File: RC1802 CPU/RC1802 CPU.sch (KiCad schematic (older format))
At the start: 50 parts, among them J1 Mount, J2 Mount, J3 Mount, J4 Mount, J5 CONN_01X39, J6 CONN_02X20, J7 BARREL_JACK, J8 Conn_CLK, J9 Conn_Q, U1 74LS04, U2 CDP1802, U3 74LS240, U4 74LS373, U5 SLOT-1, U6 SLOT-2, X1 CXO_DIP14

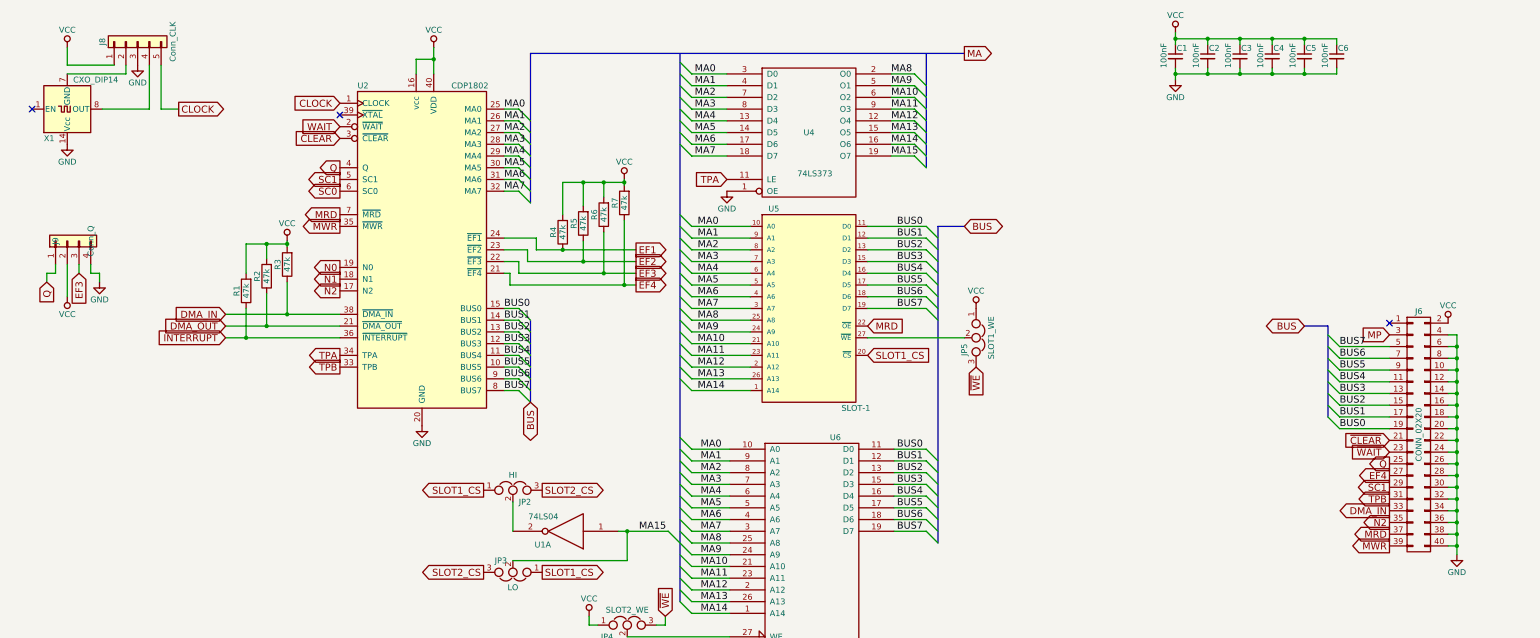
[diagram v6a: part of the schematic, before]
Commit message: Accidentally swapped VCC and GND on oscillator, no wonder it didn't work :-(
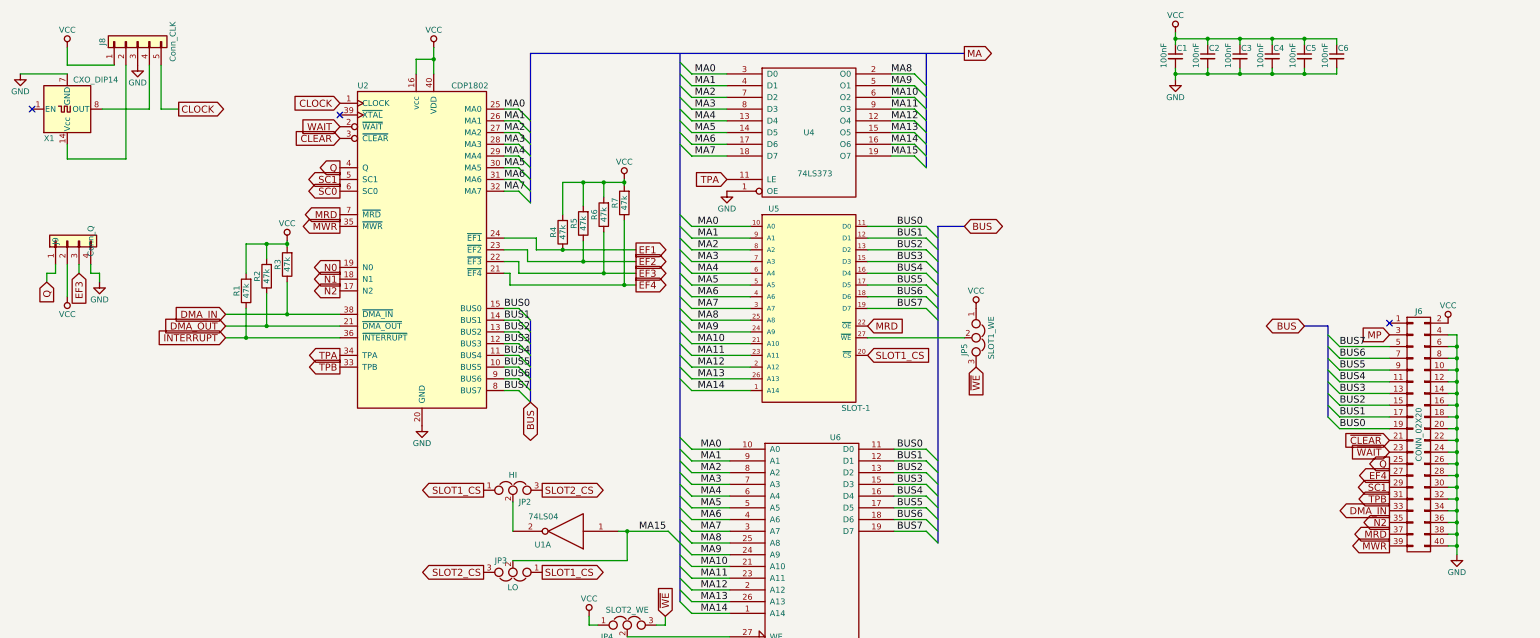
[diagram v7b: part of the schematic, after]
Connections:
- net GND: now also X1.7 (GND); no longer X1.14 (Vcc)
- net at J8.2 (Pin_2): now also X1.14 (Vcc); no longer X1.7 (GND)

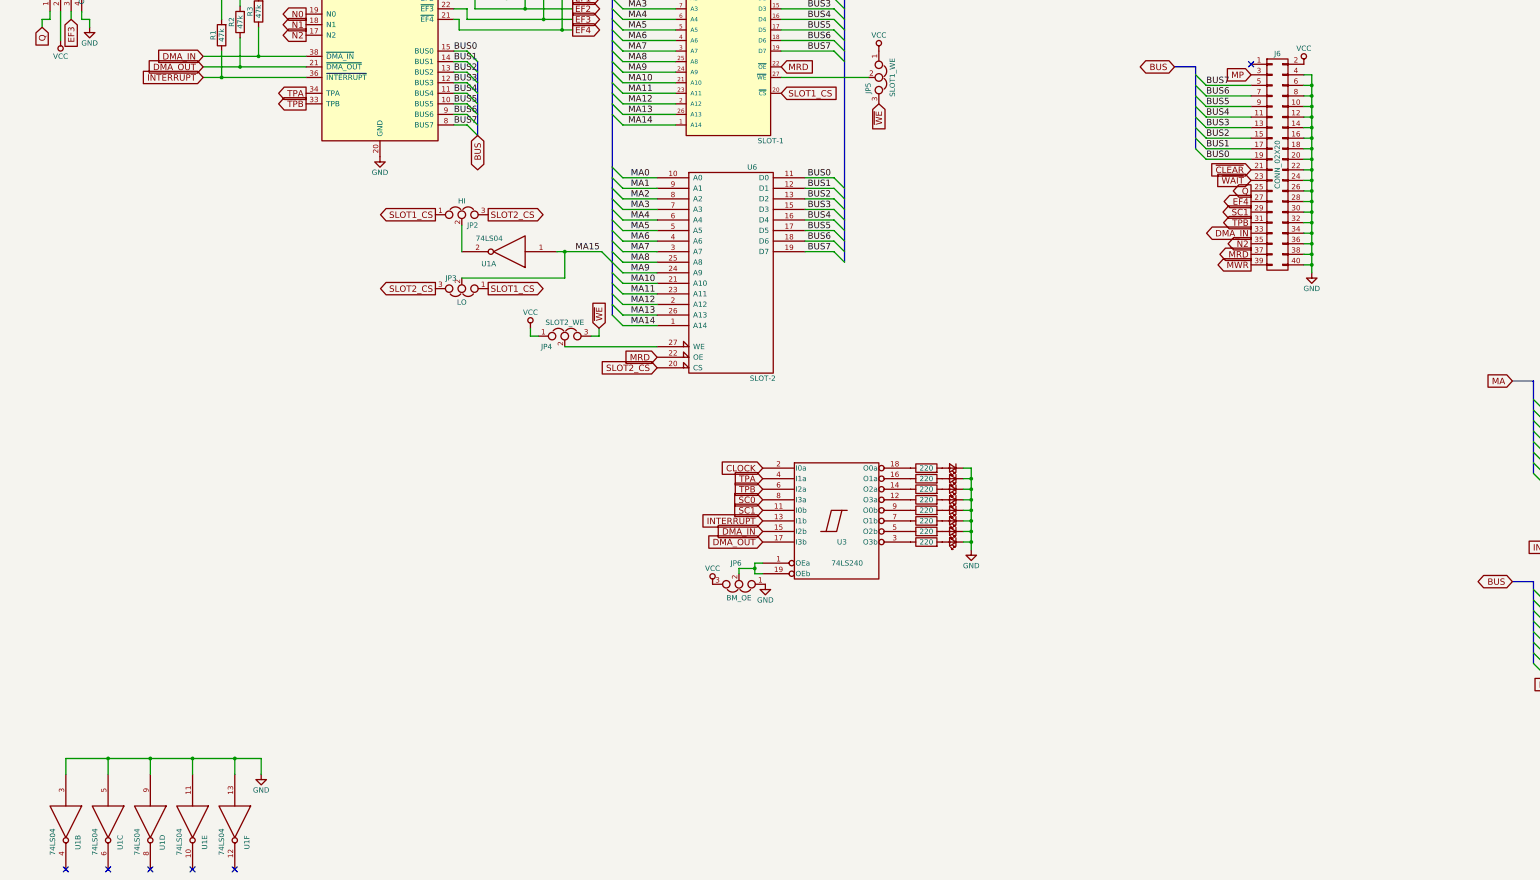
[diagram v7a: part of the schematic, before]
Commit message: Added ~Q to UI connector
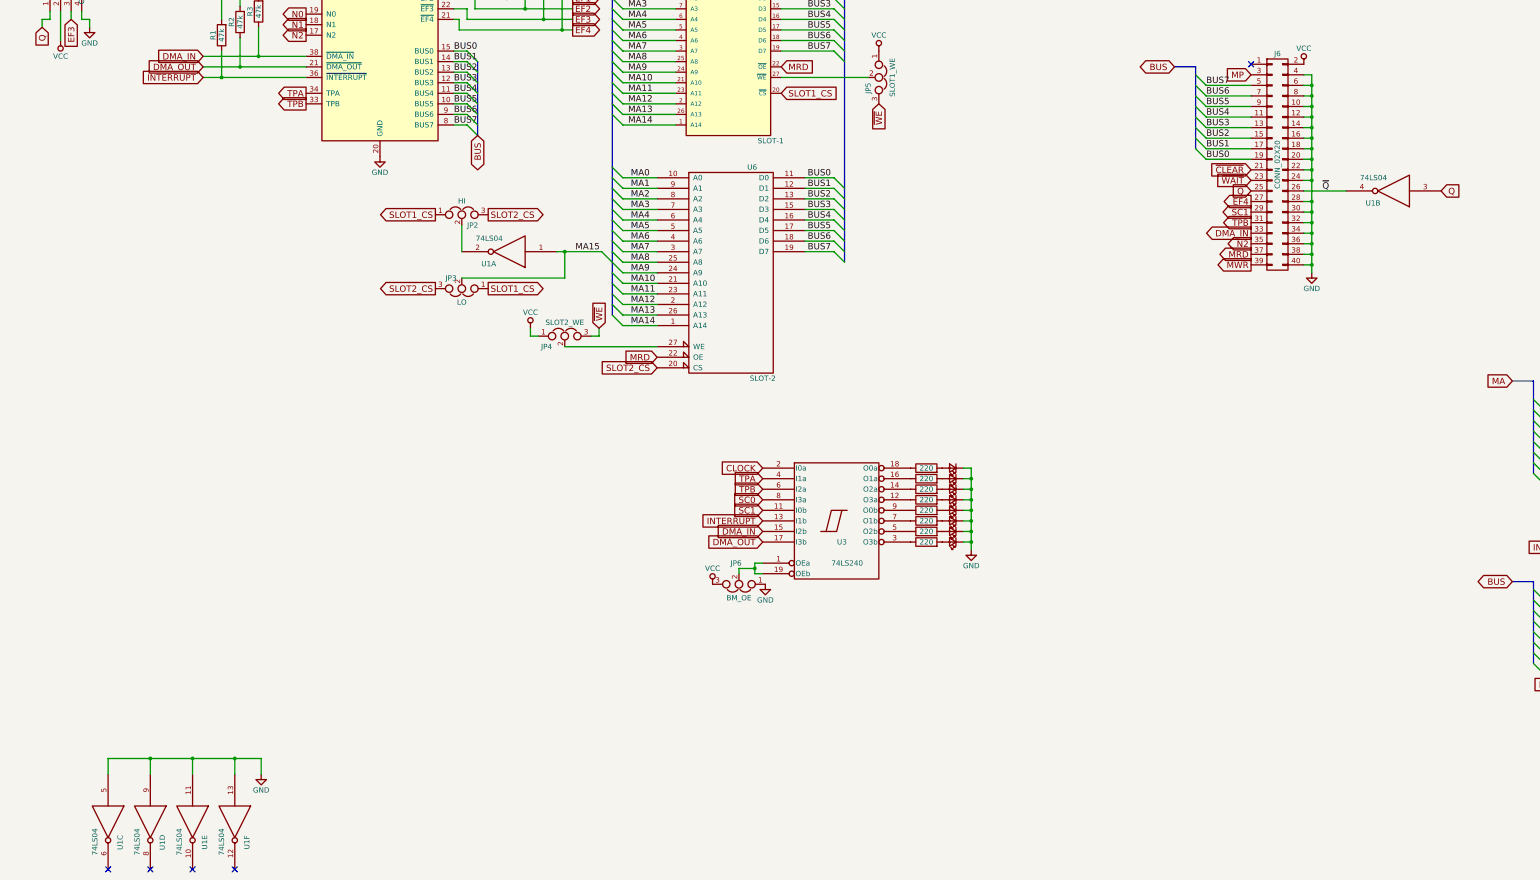
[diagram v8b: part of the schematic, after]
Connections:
- net GND: no longer J6.26 (P26), U1.3
- net Q: now also U1.3
- net ~Q: now reaches U1.4
- net ~Q: now also J6.26 (P26)
- no-connect marks 13 -> 12
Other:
- moved on the sheet: U1B
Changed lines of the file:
@@
 Text GLabel 12375 4925 0    60   Output ~ 0
 TPB
-Text GLabel 12375 4625 0    60   Output ~ 0
+Text GLabel 12375 4625 0    60   Input ~ 0
 Q
 Text GLabel 12375 4425 0    60   Input ~ 0
@@
 L 74LS04 U1
 U 2 1 5B22F8BE
-P 1150 10600
-F 0 "U1" H 1345 10715 50  0000 C CNN
-F 1 "74LS04" H 1340 10475 50  0000 C CNN
-F 2 "Housings_DIP:DIP-14_W7.62mm_Socket" H 1150 10600 50  0001 C CNN
-F 3 "" H 1150 10600 50  0001 C CNN
-	2    1150 10600
-	0    1    1    0
+P 13725 4625
+F 0 "U1" H 13920 4740 50  0000 C CNN
+F 1 "74LS04" H 13915 4500 50  0000 C CNN
+F 2 "Housings_DIP:DIP-14_W7.62mm_Socket" H 13725 4625 50  0001 C CNN
+F 3 "" H 13725 4625 50  0001 C CNN
+	2    13725 4625
+	-1   0    0    1
 $EndComp
 $Comp
@@
 	0    1    1    0
 $EndComp
-NoConn ~ 1150 11050
 NoConn ~ 1550 11050
 NoConn ~ 1950 11050
@@
 	12950 3525 12950 5400
 Wire Wire Line
-	12950 3525 12875 3525
-Wire Wire Line
 	12875 3625 12950 3625
 Connection ~ 12950 3625
@@
 Connection ~ 12950 4425
 Wire Wire Line
-	12875 4525 12950 4525
+	12950 4525 12875 4525
 Connection ~ 12950 4525
-Wire Wire Line
-	12875 4625 12950 4625
-Connection ~ 12950 4625
 Wire Wire Line
 	12875 4725 12950 4725
@@
 	10550 1300 11925 1300
 Wire Wire Line
-	1150 10150 1150 10000
-Wire Wire Line
-	1150 10000 3000 10000
+	1550 10000 3000 10000
 Wire Wire Line
 	3000 10000 3000 10150
@@
 Connection ~ 1950 10000
 Wire Wire Line
-	1550 10150 1550 10000
-Connection ~ 1550 10000
-Wire Wire Line
 	7925 3550 8750 3550
 Wire Wire Line
@@
 Wire Wire Line
 	1100 2025 1100 1900
+Wire Wire Line
+	12875 3525 12950 3525
+Wire Wire Line
+	12875 4625 13275 4625
+Text GLabel 14175 4625 2    60   Input ~ 0
+Q
+Wire Wire Line
+	1550 10150 1550 10000
+Text Label 13050 4625 0    60   ~ 0
+~Q
 $EndSCHEMATC
